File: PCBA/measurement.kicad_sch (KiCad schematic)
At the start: 5 parts

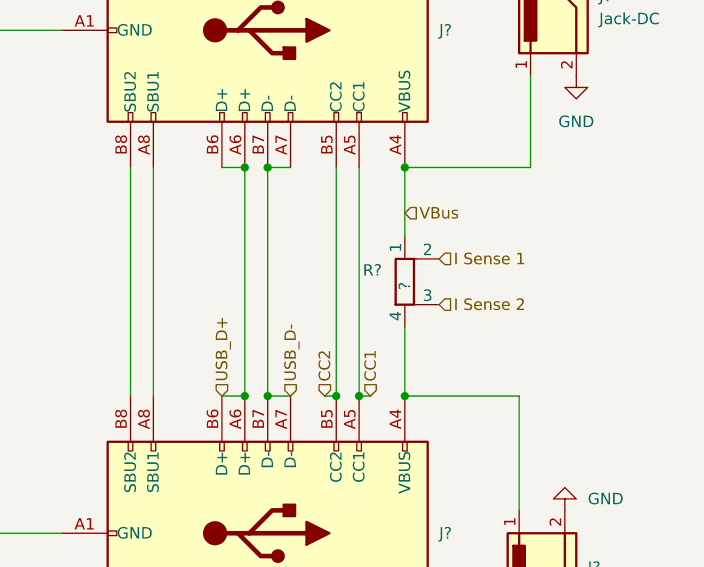
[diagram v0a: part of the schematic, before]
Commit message: ADC readings
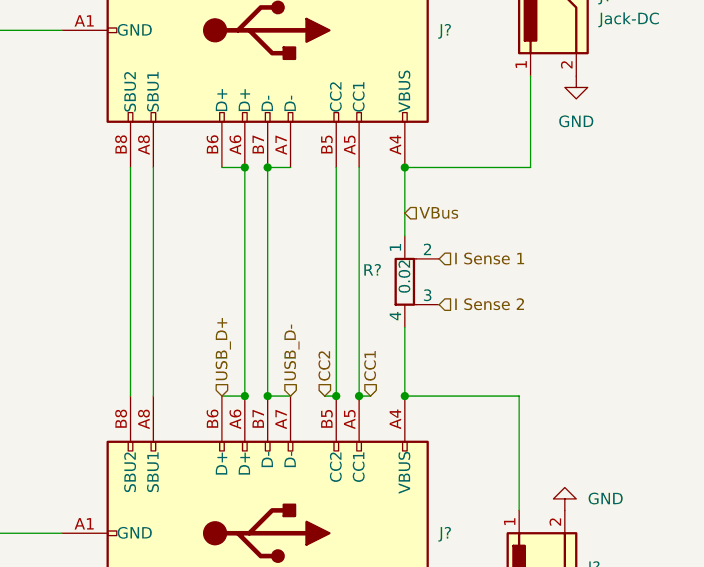
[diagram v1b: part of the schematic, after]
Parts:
- R?: value ? -> 0.02
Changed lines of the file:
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@@
       (effects (font (size 1.27 1.27)) (justify right))
     )
-    (property "Value" "?" (id 1) (at 149.86 92.71 90)
+    (property "Value" "0.02" (id 1) (at 149.86 90.17 90)
       (effects (font (size 1.27 1.27)) (justify right))
     )

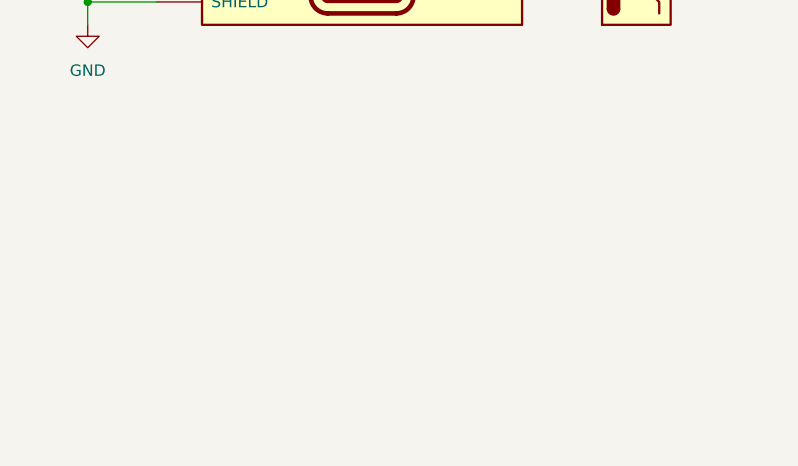
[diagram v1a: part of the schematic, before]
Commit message: TODO: usb c plug
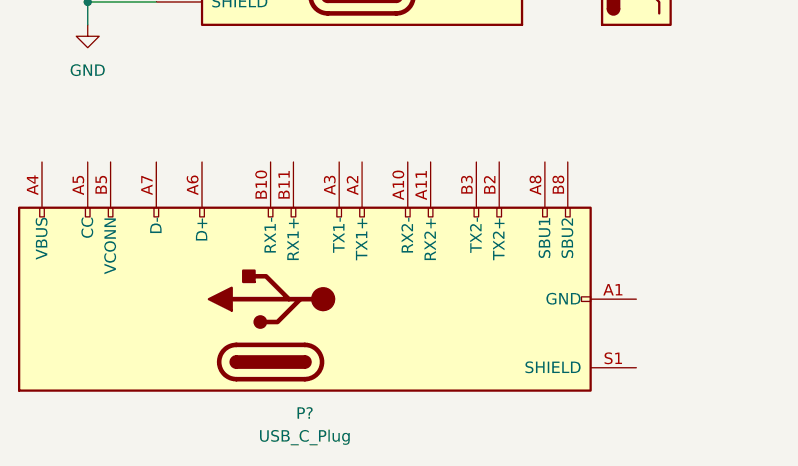
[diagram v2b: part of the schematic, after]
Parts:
- added P?: USB_C_Plug, symbol Connector:USB_C_Plug
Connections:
- new net: P?.A1 (GND), P?.A12 (GND), P?.B1 (GND), P?.B12 (GND)
- new net: P?.A4 (VBUS), P?.A9 (VBUS), P?.B4 (VBUS), P?.B9 (VBUS)
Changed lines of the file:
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@@
     (pin "4")
+  )
+  (symbol (lib_id "Connector:USB_C_Plug") (at 124.46 161.29 90) (unit 1)
+    (in_bom yes) (on_board yes) (fields_autoplaced)
+    (property "Reference" "P?" (id 0) (at 128.27 173.99 90))
+    (property "Value" "USB_C_Plug" (id 1) (at 128.27 176.53 90))
+    (property "Footprint" "" (id 2) (at 124.46 157.48 0)
+      (effects (font (size 1.27 1.27)) hide)
+    )
+    (property "Datasheet" "https://www.usb.org/sites/default/files/documents/usb_type-c.zip" (id 3) (at 124.46 157.48 0)
+      (effects (font (size 1.27 1.27)) hide)
+    )
+    (pin "A1")
+    (pin "A10")
+    (pin "A11")
+    (pin "A12")
+    (pin "A2")
+    (pin "A3")
+    (pin "A4")
+    (pin "A5")
+    (pin "A6")
+    (pin "A7")
+    (pin "A8")
+    (pin "A9")
+    (pin "B1")
+    (pin "B10")
+    (pin "B11")
+    (pin "B12")
+    (pin "B2")
+    (pin "B3")
+    (pin "B4")
+    (pin "B5")
+    (pin "B8")
+    (pin "B9")
+    (pin "S1")
   )
   (symbol (lib_id "Connector:Jack-DC") (at 166.37 62.23 90) (mirror x) (unit 1)

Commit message: Right usb end
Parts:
- removed J?: USB_C_Receptacle_USB2.0, symbol Connector:USB_C_Receptacle_USB2.0
- removed P?: USB_C_Plug, symbol Connector:USB_C_Plug
- added J?: USB_C_Receptacle, symbol Connector:USB_C_Receptacle
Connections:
- net CC1: now also J?.A5 (CC1)
- net CC2: now also J?.B5 (CC2)
- net GND: now also J?.A1 (GND), J?.A12 (GND), J?.B1 (GND), J?.B12 (GND), J?.S1 (SHIELD)
- net USB_D+: now also J?.A6 (D+), J?.B6 (D+)
- net USB_D-: now also J?.A7 (D-), J?.B7 (D-)
- net at J?.A8 (SBU1): now also J?.A8 (SBU1)
- net at J?.B8 (SBU2): now also J?.B8 (SBU2)
- net at J?.1, R?.4: now also J?.A4 (VBUS), J?.A9 (VBUS), J?.B4 (VBUS), J?.B9 (VBUS)
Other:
- note added: "I know this is wrong type, but Kicad schematic symbol is simplified otherwise"
- note added: "TODO? Do we have a load switch in here?"
- note added: "Thinking we might take these off and instead have an extra PCB for them or adapters.."

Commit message: More schematics
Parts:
- J501: renamed from J?; footprint (none) -> Connector_USB:USB_C_Plug_JAE_DX07P024AJ1
- J502: renamed from J?; footprint (none) -> Connector_USB:USB_C_Receptacle_HRO_TYPE-C-31-M-12
- gave numbers to parts that had none: 3
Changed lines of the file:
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@@
   (symbol (lib_id "power:GND") (at 168.91 69.85 0) (unit 1)
     (in_bom yes) (on_board yes) (fields_autoplaced)
-    (property "Reference" "#PWR?" (id 0) (at 168.91 76.2 0)
+    (property "Reference" "#PWR0130" (id 0) (at 168.91 76.2 0)
       (effects (font (size 1.27 1.27)) hide)
     )
@@
   (symbol (lib_id "power:GND") (at 104.14 64.77 0) (unit 1)
     (in_bom yes) (on_board yes) (fields_autoplaced)
-    (property "Reference" "#PWR?" (id 0) (at 104.14 71.12 0)
+    (property "Reference" "#PWR0131" (id 0) (at 104.14 71.12 0)
       (effects (font (size 1.27 1.27)) hide)
     )
@@
   (symbol (lib_id "Connector:USB_C_Receptacle_USB2.0") (at 134.62 64.77 270) (unit 1)
     (in_bom yes) (on_board yes) (fields_autoplaced)
-    (property "Reference" "J?" (id 0) (at 153.67 64.7699 90)
+    (property "Reference" "J502" (id 0) (at 153.67 64.7699 90)
       (effects (font (size 1.27 1.27)) (justify left))
     )
@@
       (effects (font (size 1.27 1.27)) (justify left) hide)
     )
-    (property "Footprint" "" (id 2) (at 134.62 68.58 0)
+    (property "Footprint" "Connector_USB:USB_C_Receptacle_HRO_TYPE-C-31-M-12" (id 2) (at 134.62 68.58 0)
       (effects (font (size 1.27 1.27)) hide)
     )
@@
   (symbol (lib_id "Connector:Jack-DC") (at 165.1 125.73 90) (unit 1)
     (in_bom yes) (on_board yes) (fields_autoplaced)
-    (property "Reference" "J?" (id 0) (at 170.18 124.4599 90)
+    (property "Reference" "J503" (id 0) (at 170.18 124.4599 90)
       (effects (font (size 1.27 1.27)) (justify right))
     )
@@
   (symbol (lib_id "Connector:USB_C_Receptacle") (at 124.46 120.65 270) (mirror x) (unit 1)
     (in_bom yes) (on_board yes) (fields_autoplaced)
-    (property "Reference" "J?" (id 0) (at 120.65 133.35 90))
+    (property "Reference" "J501" (id 0) (at 120.65 133.35 90))
     (property "Value" "USB_C_Receptacle" (id 1) (at 120.65 135.89 90))
-    (property "Footprint" "" (id 2) (at 124.46 116.84 0)
+    (property "Footprint" "Connector_USB:USB_C_Plug_JAE_DX07P024AJ1" (id 2) (at 124.46 116.84 0)
       (effects (font (size 1.27 1.27)) hide)
     )
@@
   (symbol (lib_id "power:GND") (at 167.64 118.11 180) (unit 1)
     (in_bom yes) (on_board yes) (fields_autoplaced)
-    (property "Reference" "#PWR?" (id 0) (at 167.64 111.76 0)
+    (property "Reference" "#PWR0129" (id 0) (at 167.64 111.76 0)
       (effects (font (size 1.27 1.27)) hide)
     )
@@
   (symbol (lib_id "Device:R_Shunt") (at 149.86 92.71 0) (unit 1)
     (in_bom yes) (on_board yes)
-    (property "Reference" "R?" (id 0) (at 147.32 91.4399 0)
+    (property "Reference" "R501" (id 0) (at 147.32 91.4399 0)
       (effects (font (size 1.27 1.27)) (justify right))
     )
@@
   (symbol (lib_id "Connector:Jack-DC") (at 166.37 62.23 90) (mirror x) (unit 1)
     (in_bom yes) (on_board yes) (fields_autoplaced)
-    (property "Reference" "J?" (id 0) (at 171.45 60.9599 90)
+    (property "Reference" "J504" (id 0) (at 171.45 60.9599 90)
       (effects (font (size 1.27 1.27)) (justify right))
     )
@@
   (symbol (lib_id "power:GND") (at 83.82 128.27 0) (unit 1)
     (in_bom yes) (on_board yes) (fields_autoplaced)
-    (property "Reference" "#PWR?" (id 0) (at 83.82 134.62 0)
+    (property "Reference" "#PWR0132" (id 0) (at 83.82 134.62 0)
       (effects (font (size 1.27 1.27)) hide)
     )

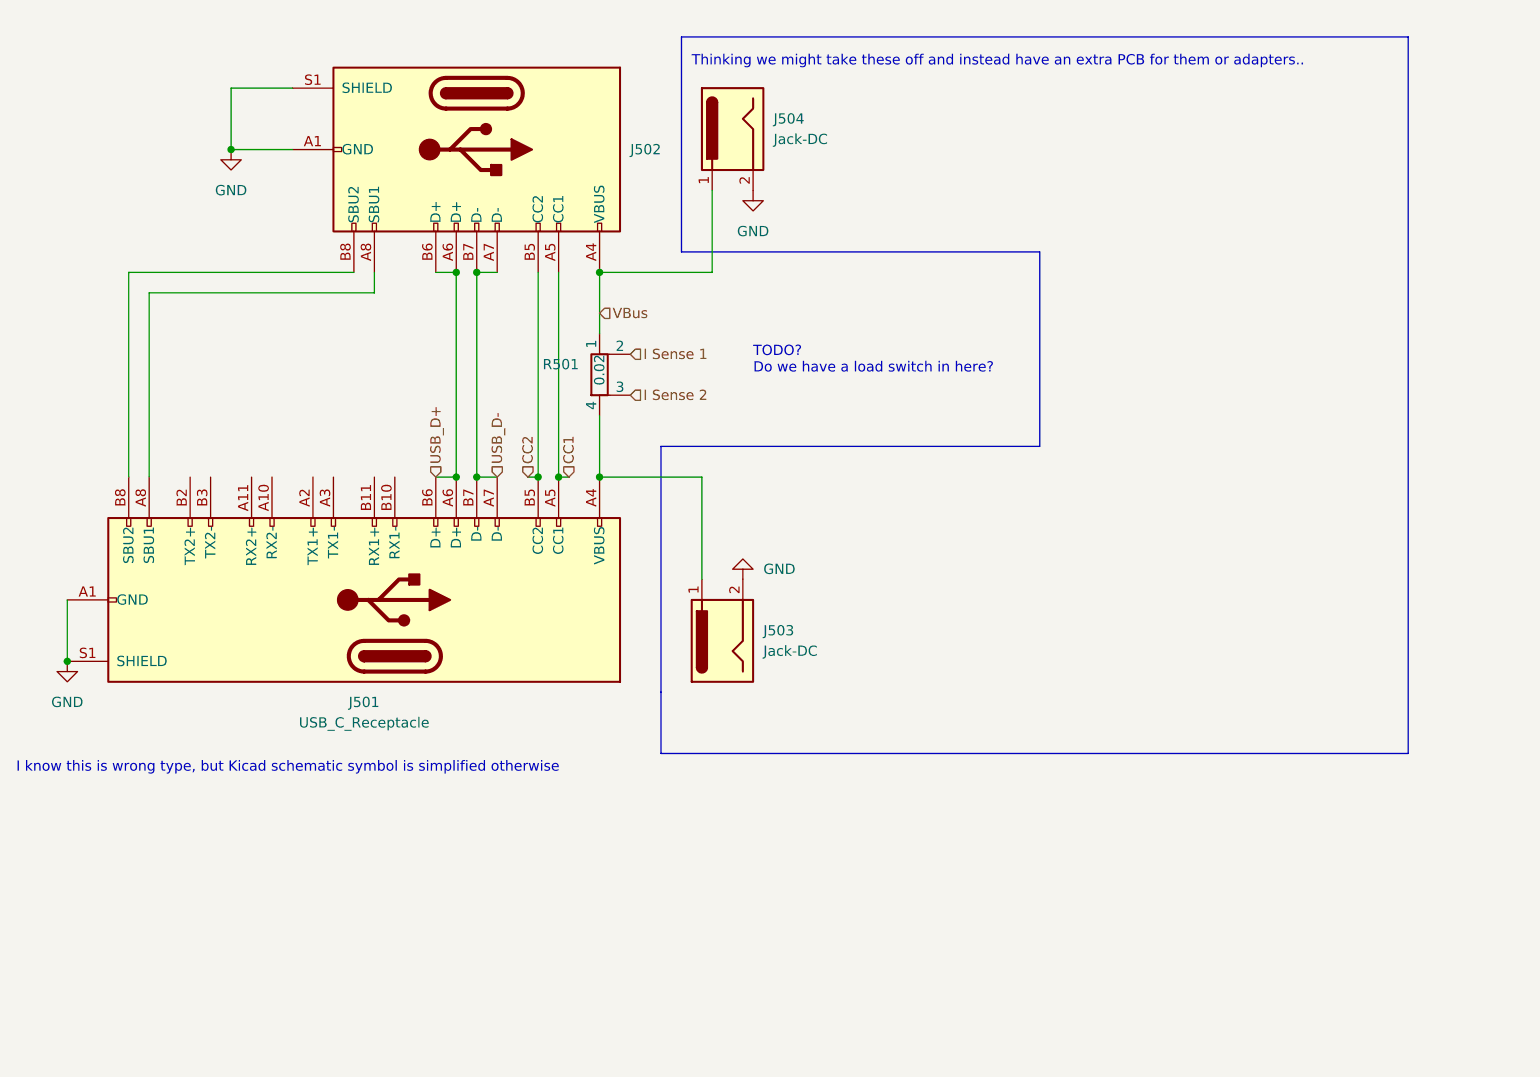
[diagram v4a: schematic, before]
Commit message: Update schematic pinmap bl706
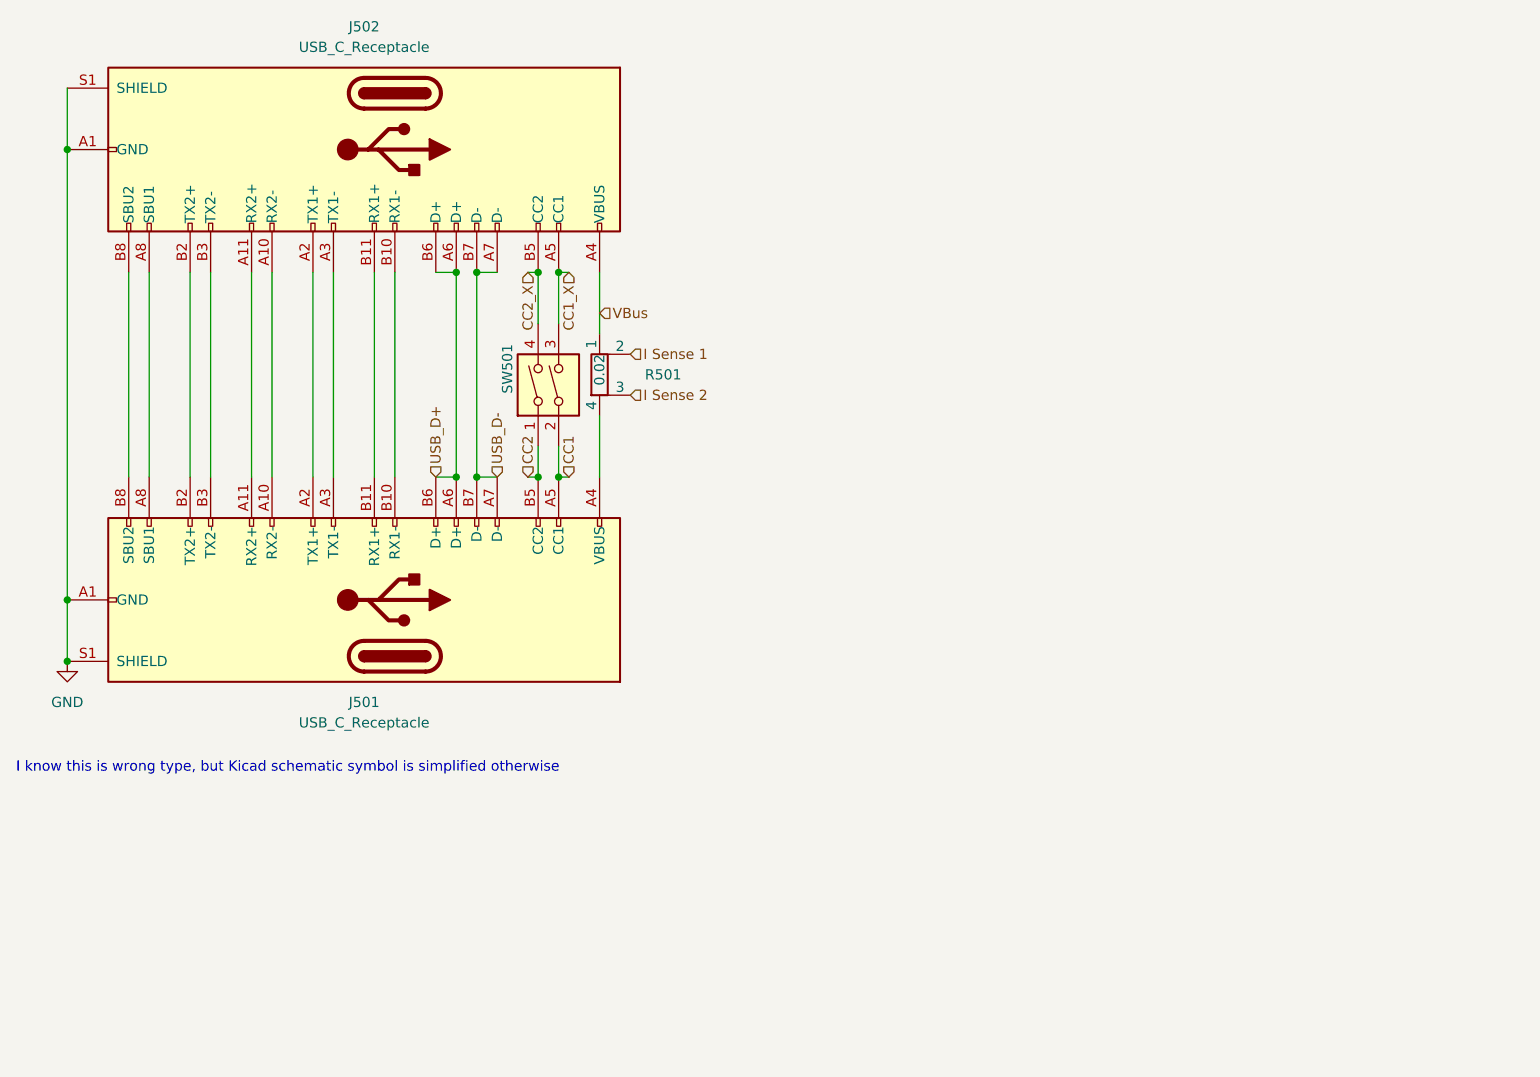
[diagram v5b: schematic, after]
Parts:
- removed J502: USB_C_Receptacle_USB2.0, Connector_USB:USB_C_Receptacle_HRO_TYPE-C-31-M-12, symbol Connector:USB_C_Receptacle_USB2.0
- removed J503, J504: Jack-DC, symbol Connector:Jack-DC
- added J502: USB_C_Receptacle, Connector_USB:USB_C_Receptacle_Amphenol_12401610E4-2A, symbol Connector:USB_C_Receptacle
- added SW501: SW_DIP_x02, symbol Switch:SW_DIP_x02
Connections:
- net CC1: now also SW501.2
- net CC2: now also SW501.1
- net GND: now also J502.A1 (GND), J502.A12 (GND), J502.B1 (GND), J502.B12 (GND), J502.S1 (SHIELD)
- net USB_D+: now also J502.A6 (D+), J502.B6 (D+)
- net USB_D-: now also J502.A7 (D-), J502.B7 (D-)
- net VBus: now also J502.A4 (VBUS), J502.A9 (VBUS), J502.B4 (VBUS), J502.B9 (VBUS)
- net at J501.A8 (SBU1): now also J502.A8 (SBU1)
- net at J501.B8 (SBU2): now also J502.B8 (SBU2)
- net at J501.A10 (RX2-): now also J502.A10 (RX2-)
- net at J501.A11 (RX2+): now also J502.A11 (RX2+)
- net at J501.A2 (TX1+): now also J502.A2 (TX1+)
- net at J501.A3 (TX1-): now also J502.A3 (TX1-)
- net at J501.B10 (RX1-): now also J502.B10 (RX1-)
- net at J501.B11 (RX1+): now also J502.B11 (RX1+)
- net at J501.B2 (TX2+): now also J502.B2 (TX2+)
- net at J501.B3 (TX2-): now also J502.B3 (TX2-)
- new net CC1_X: J502.A5 (CC1), SW501.3
- new net CC2_X: J502.B5 (CC2), SW501.4
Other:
- note removed: "TODO? Do we have a load switch in here?"
- note removed: "Thinking we might take these off and instead have an extra PCB for them or adapters.."

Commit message: Rough outline
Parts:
- R501: footprint (none) -> Resistor_SMD:R_Shunt_Vishay_WSK2512_6332Metric_T1.19mm
- SW501: footprint (none) -> Button_Switch_SMD:SW_DIP_SPSTx02_Slide_Copal_CHS-02A_W5.08mm_P1.27mm_JPin
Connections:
- net CC1: now also SW501.1; no longer SW501.2
- net CC1_X: now also SW501.4; no longer SW501.3
- net CC2: now also SW501.2; no longer SW501.1
- net CC2_X: now also SW501.3; no longer SW501.4
- net RX2_-: now reaches J501.A10 (RX2-), J502.A10 (RX2-)
- net RX2_+: now reaches J501.A11 (RX2+), J502.A11 (RX2+)
- net TX1_+: now reaches J501.A2 (TX1+), J502.A2 (TX1+)
- net TX1_-: now reaches J501.A3 (TX1-), J502.A3 (TX1-)
- net SBU1: now reaches J501.A8 (SBU1), J502.A8 (SBU1)
- net RX1_-: now reaches J501.B10 (RX1-), J502.B10 (RX1-)
- net RX1_+: now reaches J501.B11 (RX1+), J502.B11 (RX1+)
- net TX2_+: now reaches J501.B2 (TX2+), J502.B2 (TX2+)
- net TX2_-: now reaches J501.B3 (TX2-), J502.B3 (TX2-)
- net SBU2: now reaches J501.B8 (SBU2), J502.B8 (SBU2)
- net VBUS2: now reaches J501.A4 (VBUS), J501.A9 (VBUS), J501.B4 (VBUS), J501.B9 (VBUS), R501.4
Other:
- moved on the sheet: SW501
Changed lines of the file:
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@@
+    (effects (font (size 1.27 1.27)) (justify left bottom))
+  )
+  (label "TX2_-" (at 101.6 105.41 90)
+    (effects (font (size 1.27 1.27)) (justify left bottom))
+  )
+  (label "SBU1" (at 93.98 105.41 90)
+    (effects (font (size 1.27 1.27)) (justify left bottom))
+  )
+  (label "TX1_-" (at 116.84 105.41 90)
+    (effects (font (size 1.27 1.27)) (justify left bottom))
+  )
+  (label "VBUS2" (at 149.86 102.87 0)
+    (effects (font (size 1.27 1.27)) (justify left bottom))
+  )
+  (label "SBU2" (at 91.44 105.41 90)
+    (effects (font (size 1.27 1.27)) (justify left bottom))
+  )
+  (label "RX2_+" (at 106.68 105.41 90)
+    (effects (font (size 1.27 1.27)) (justify left bottom))
+  )
+  (label "TX1_+" (at 114.3 105.41 90)
+    (effects (font (size 1.27 1.27)) (justify left bottom))
+  )
+  (label "RX2_-" (at 109.22 105.41 90)
+    (effects (font (size 1.27 1.27)) (justify left bottom))
+  )
+  (label "RX1_+" (at 121.92 105.41 90)
+    (effects (font (size 1.27 1.27)) (justify left bottom))
+  )
+  (label "TX2_+" (at 99.06 105.41 90)
+    (effects (font (size 1.27 1.27)) (justify left bottom))
+  )
+  (label "RX1_-" (at 124.46 105.41 90)
     (effects (font (size 1.27 1.27)) (justify left bottom))
   )
@@
       (effects (font (size 1.27 1.27)) (justify right))
     )
-    (property "Footprint" "" (id 2) (at 148.082 92.71 90)
+    (property "Footprint" "Resistor_SMD:R_Shunt_Vishay_WSK2512_6332Metric_T1.19mm" (id 2) (at 148.082 92.71 90)
       (effects (font (size 1.27 1.27)) hide)
     )
@@
     (pin "4")
   )
-  (symbol (lib_id "Switch:SW_DIP_x02") (at 144.78 93.98 90) (unit 1)
+  (symbol (lib_id "Switch:SW_DIP_x02") (at 142.24 93.98 270) (mirror x) (unit 1)
     (in_bom yes) (on_board yes)
-    (property "Reference" "SW501" (id 0) (at 138.43 88.9 0)
+    (property "Reference" "SW501" (id 0) (at 148.59 88.9 0)
       (effects (font (size 1.27 1.27)) (justify right))
     )
-    (property "Value" "SW_DIP_x02" (id 1) (at 148.59 95.2499 90)
+    (property "Value" "SW_DIP_x02" (id 1) (at 138.43 95.2499 90)
       (effects (font (size 1.27 1.27)) (justify right) hide)
     )
-    (property "Footprint" "" (id 2) (at 144.78 93.98 0)
+    (property "Footprint" "Button_Switch_SMD:SW_DIP_SPSTx02_Slide_Copal_CHS-02A_W5.08mm_P1.27mm_JPin" (id 2) (at 142.24 93.98 0)
       (effects (font (size 1.27 1.27)) hide)
     )
-    (property "Datasheet" "~" (id 3) (at 144.78 93.98 0)
+    (property "Datasheet" "~" (id 3) (at 142.24 93.98 0)
       (effects (font (size 1.27 1.27)) hide)
     )

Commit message: Finish routing
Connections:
- net VBUS2: now also J502.A4 (VBUS), J502.A9 (VBUS), J502.B4 (VBUS), J502.B9 (VBUS), R501.1; no longer J501.A4 (VBUS), J501.A9 (VBUS), J501.B4 (VBUS), J501.B9 (VBUS), R501.4
- net VBus: now also J501.A4 (VBUS), J501.A9 (VBUS), J501.B4 (VBUS), J501.B9 (VBUS), R501.4; no longer J502.A4 (VBUS), J502.A9 (VBUS), J502.B4 (VBUS), J502.B9 (VBUS), R501.1
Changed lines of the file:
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@@
     (effects (font (size 1.27 1.27)) (justify left bottom))
   )
-  (label "VBUS2" (at 149.86 102.87 0)
+  (label "VBUS2" (at 149.86 85.09 0)
     (effects (font (size 1.27 1.27)) (justify left bottom))
   )
@@
     (effects (font (size 1.27 1.27)) (justify left))
   )
-  (hierarchical_label "VBus" (shape input) (at 149.86 85.09 0)
+  (hierarchical_label "VBus" (shape input) (at 149.86 102.87 0)
     (effects (font (size 1.27 1.27)) (justify left))
   )
